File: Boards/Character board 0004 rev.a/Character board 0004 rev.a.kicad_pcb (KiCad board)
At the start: 2 copper layers, 184.3 x 186.8 mm, 64 parts, among them J1 card edge, J2 character connector, Q1 2N6125, U1 2.2K, U10 Unused DIP, U11 ULN2003A, U12 ULN2003A, U13 7406, U14 74LS42, U15 LM741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

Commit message: updated boards to have correct logos
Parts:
- added G1: GND, Evan's parts:PTT white, F.Cu at (72.4, 27.3)
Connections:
- net BCLK renamed aux1_AGC
- net UNUSED1 renamed aux2_AGC
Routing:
- net GND: track 578.6 -> 606.3 mm

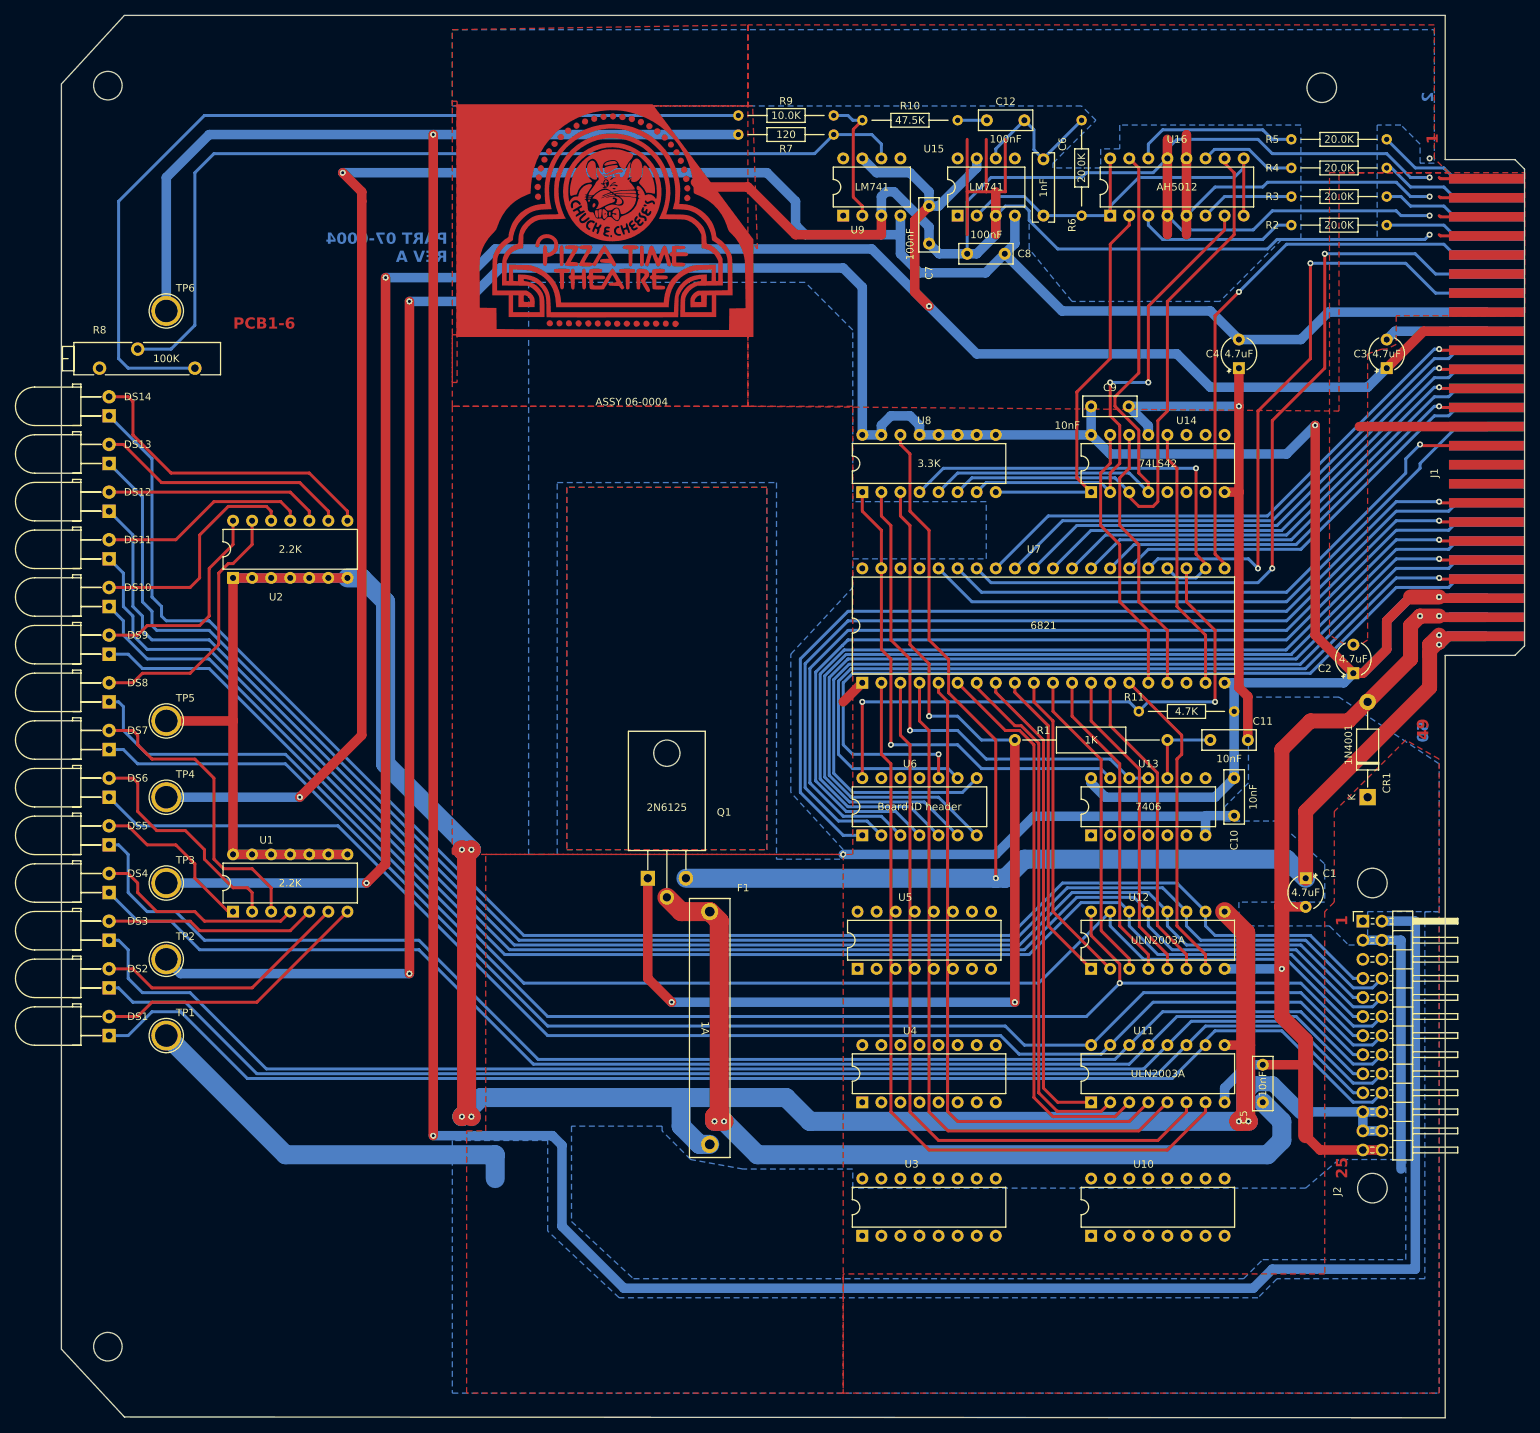
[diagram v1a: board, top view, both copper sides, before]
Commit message: revised LED spacing rev a
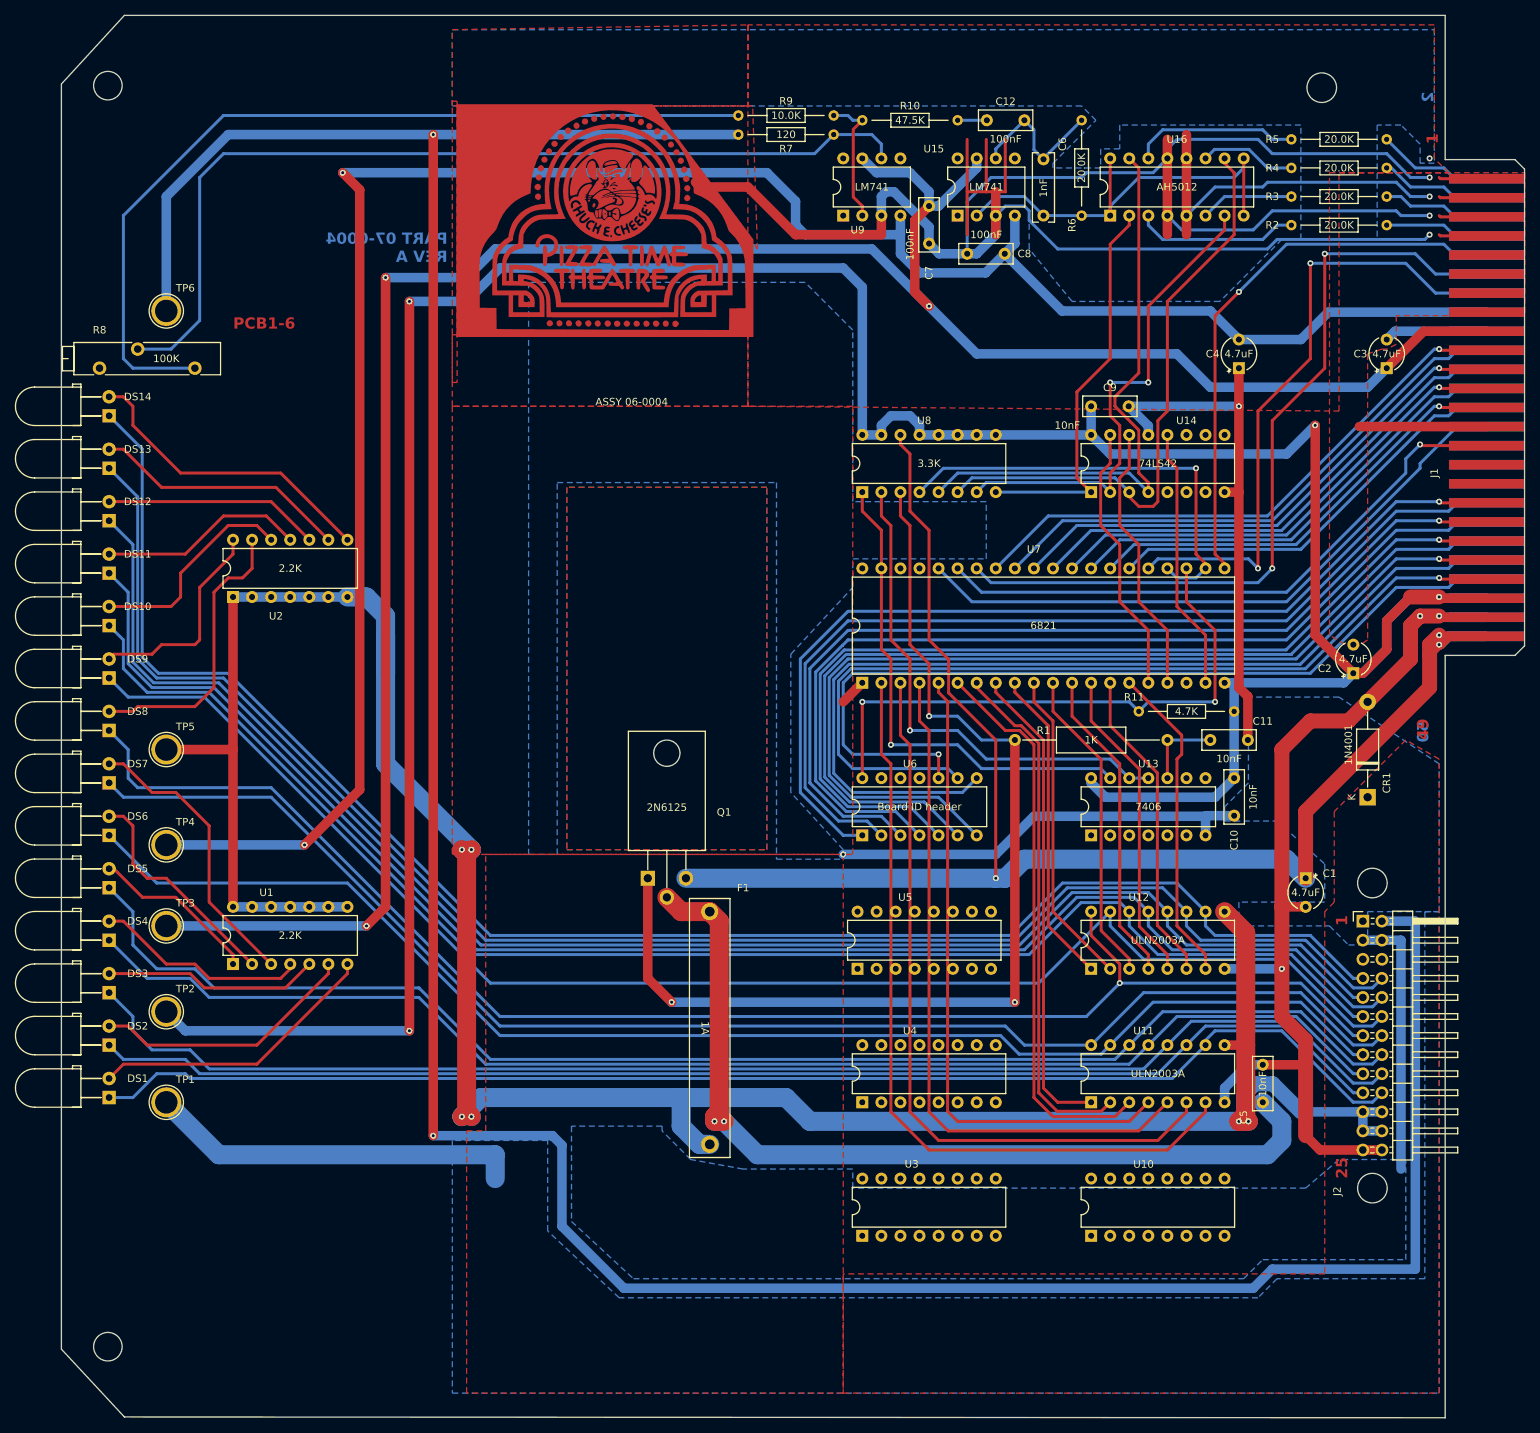
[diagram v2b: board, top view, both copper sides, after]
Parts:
- moved TP1 8.89 mm to (14.0, 144.8)
- moved DS1 8.25 mm to (6.35, 141.6)
- moved DS2 7.62 mm to (6.35, 134.6)
- moved DS3 6.98 mm to (6.35, 127.6)
- moved TP2 6.98 mm to (14.0, 132.7)
- moved U1 6.98 mm to (22.9, 126.4)
- moved DS4 6.35 mm to (6.35, 120.7)
- moved TP4 6.35 mm to (14.0, 110.5)
- moved DS5 5.72 mm to (6.35, 113.7)
- moved TP3 5.72 mm to (14.0, 121.3)
- moved DS6 5.08 mm to (6.35, 106.7)
- moved DS7 4.44 mm to (6.35, 99.7)
- moved TP5 3.81 mm to (14.0, 97.8)
- moved DS8 3.81 mm to (6.35, 92.7)
- moved DS9 3.17 mm to (6.35, 85.7)
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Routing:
- net 24Vout: track 362.9 -> 347.4 mm
- net 5V: track 409.1 -> 416.9 mm
- net -12V: track 282.1 -> 288.6 mm
- net 12V: track 304.6 -> 310.3 mm
- net B5out: track 216.5 -> 221.2 mm
- net A2out: track 185.4 -> 181.4 mm
- net GND: track 606.3 -> 602.6 mm
- net A0out: track 182.0 -> 178.6 mm
- net A1out: track 178.1 -> 174.9 mm
- net B4out: track 215.2 -> 218.3 mm
- net Net-(DS8-A): track 35.4 -> 38.2 mm
- net A4out: track 190.4 -> 187.7 mm
- net A3out: track 182.3 -> 179.6 mm
- net Net-(R8-Pad1): track 118.9 -> 116.5 mm
- net Net-(DS10-A): track 30.9 -> 28.7 mm
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
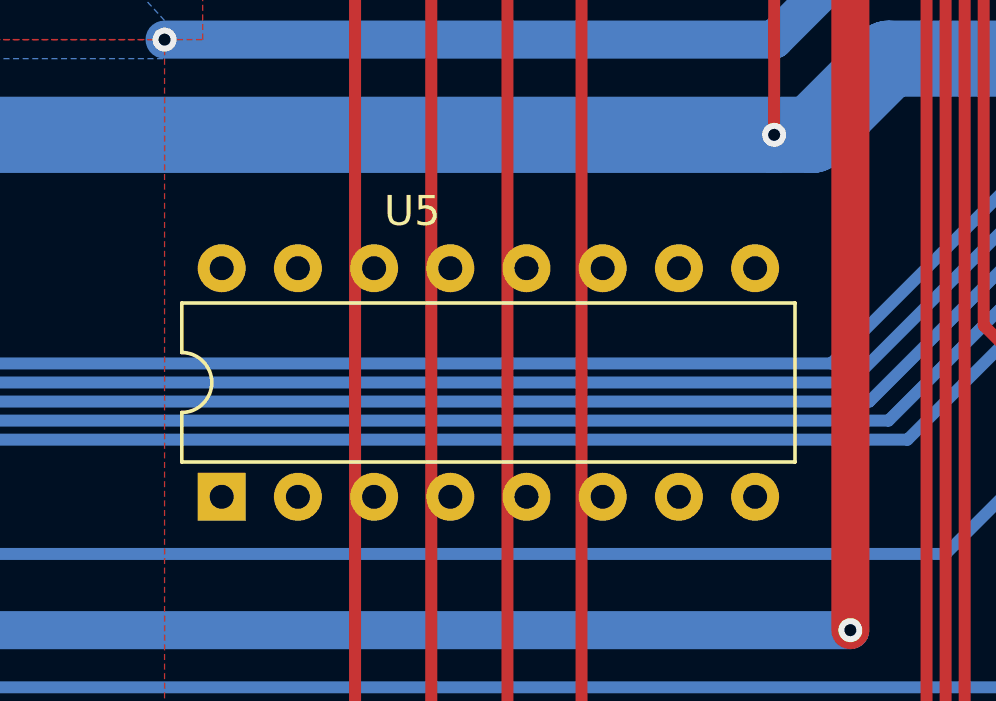
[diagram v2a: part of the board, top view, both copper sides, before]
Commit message: one chip misplaced
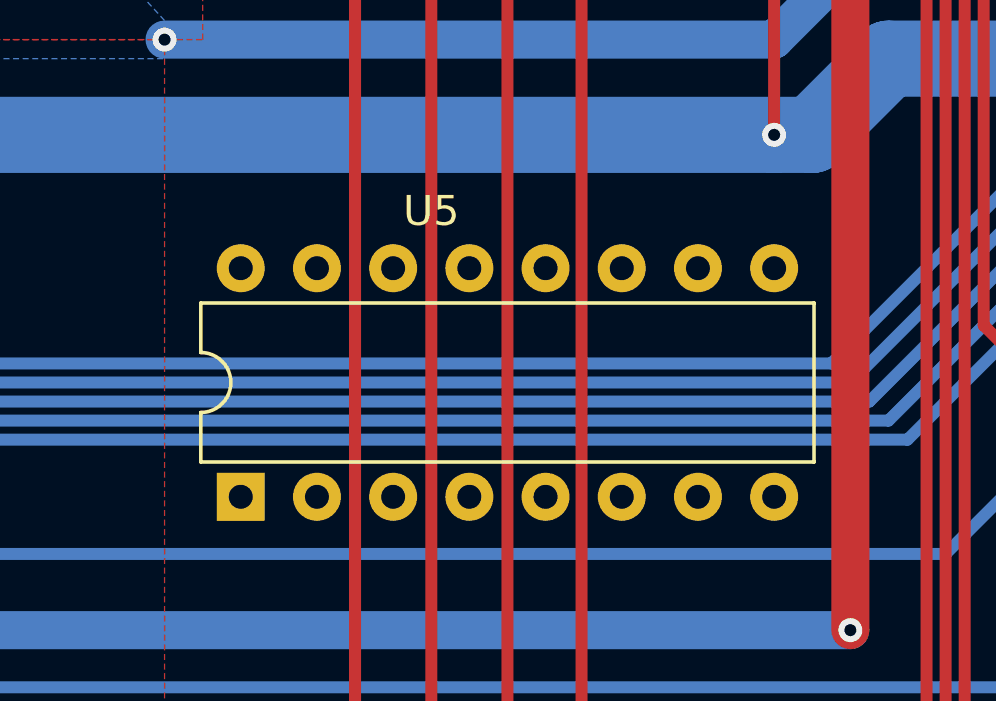
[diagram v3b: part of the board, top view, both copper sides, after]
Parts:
- moved U5 0.64 mm to (106.7, 127.0)
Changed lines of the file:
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@@
   )
   (footprint "Package_DIP:DIP-16_W7.62mm" (layer "F.Cu")
-    (at 106.045 127 90)
+    (at 106.68 127 90)
     (descr "16-lead though-hole mounted DIP package, row spacing 7.62 mm (300 mils)")
     (tags "THT DIP DIL PDIP 2.54mm 7.62mm 300mil")

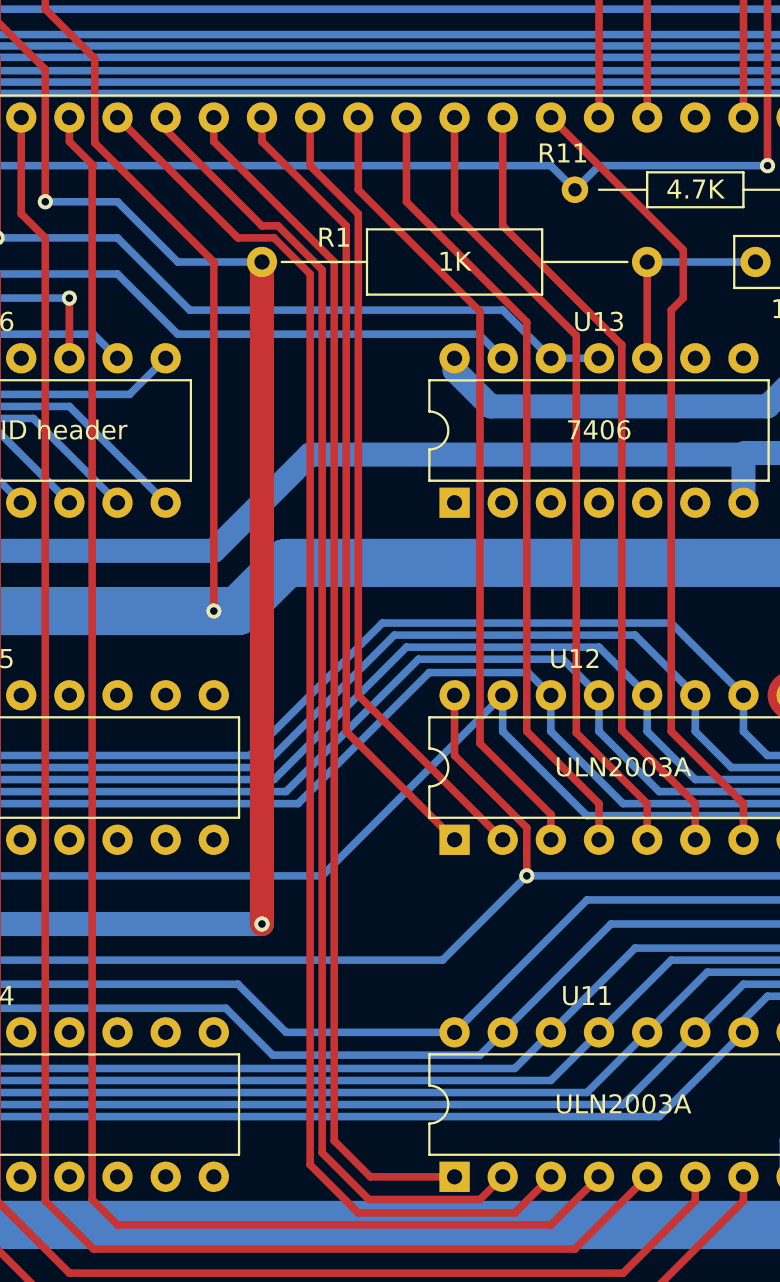
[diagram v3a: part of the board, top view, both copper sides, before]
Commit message: revisions from real life boards
tip130a is actually tip30a, widened holes for crystal, widened holes for big power resistor, fixed cpu board LED resistors
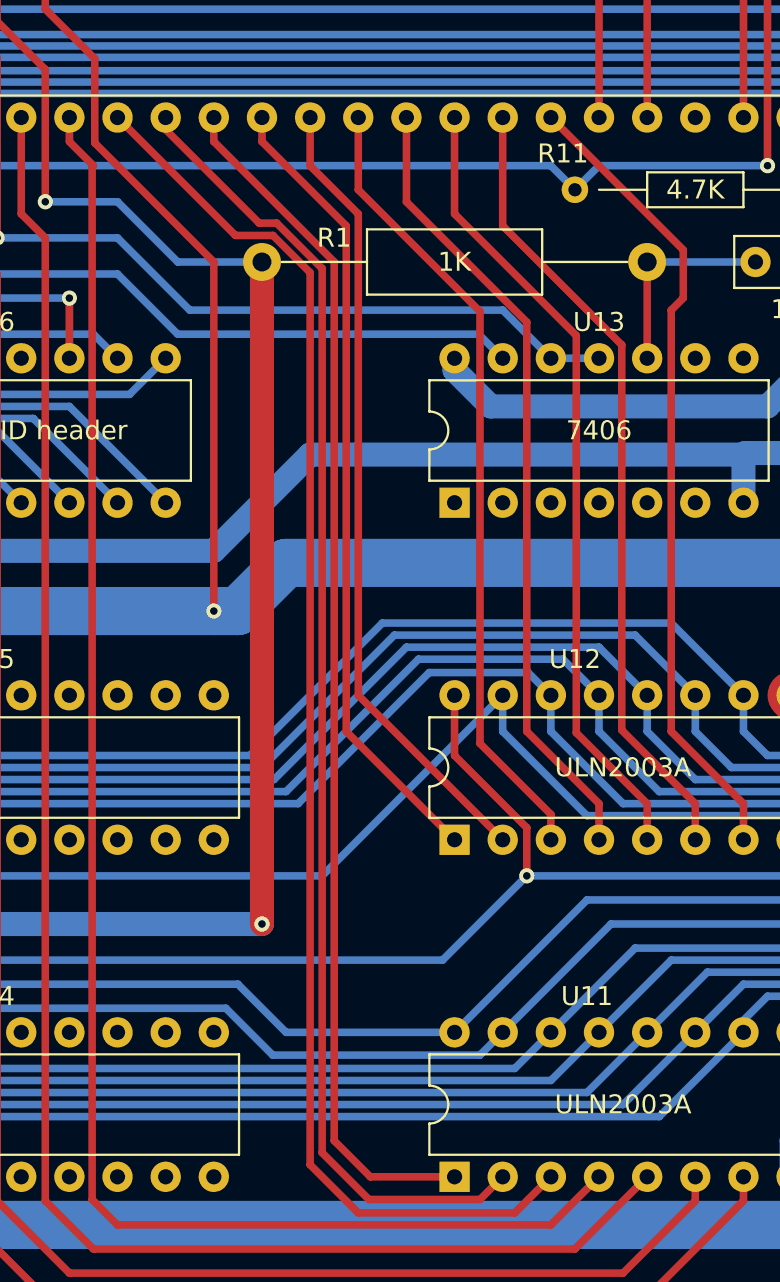
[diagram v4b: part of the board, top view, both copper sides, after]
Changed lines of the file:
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@@
     (fp_line (start 20.32 0) (end 14.66 0)
       (stroke (width 0.1) (type solid)) (layer "F.Fab"))
-    (pad "1" thru_hole circle (at 0 0) (size 1.6 1.6) (drill 0.8) (layers "*.Cu" "*.Mask")
+    (pad "1" thru_hole circle (at 0 0) (size 2 2) (drill 1) (layers "*.Cu" "*.Mask")
       (net 184 "24Vpu") (pintype "passive"))
-    (pad "2" thru_hole oval (at 20.32 0) (size 1.6 1.6) (drill 0.8) (layers "*.Cu" "*.Mask")
+    (pad "2" thru_hole circle (at 20.32 0) (size 2 2) (drill 1) (layers "*.Cu" "*.Mask")
       (net 182 "Net-(C11-Pad1)") (pintype "passive"))
     (model "${KICAD6_3DMODEL_DIR}/Resistor_THT.3dshapes/R_Axial_DIN0309_L9.0mm_D3.2mm_P20.32mm_Horizontal.wrl"
@@
   (segment (start 118.11 91.44) (end 118.04 91.51) (width 0.4) (layer "F.Cu") (net 170))
   (segment (start 116.84 90.17) (end 118.11 91.44) (width 0.4) (layer "F.Cu") (net 170))
-  (segment (start 119.38 88.9) (end 125.73 95.25) (width 0.4) (layer "F.Cu") (net 171))
-  (segment (start 125.73 95.25) (end 127.635 95.25) (width 0.4) (layer "F.Cu") (net 171))
-  (segment (start 132.08 146.685) (end 140.335 146.685) (width 0.4) (layer "F.Cu") (net 171))
-  (segment (start 140.335 146.685) (end 142.24 144.78) (width 0.4) (layer "F.Cu") (net 171))
   (segment (start 129.54 144.145) (end 132.08 146.685) (width 0.4) (layer "F.Cu") (net 171))
-  (segment (start 127.635 95.25) (end 129.54 97.155) (width 0.4) (layer "F.Cu") (net 171))
-  (segment (start 129.54 97.155) (end 129.54 144.145) (width 0.4) (layer "F.Cu") (net 171))
-  (segment (start 127.848528 94.615) (end 130.175 96.941472) (width 0.4) (layer "F.Cu") (net 172))
-  (segment (start 130.175 143.51) (end 132.645 145.98) (width 0.4) (layer "F.Cu") (net 172))
-  (segment (start 121.92 89.535) (end 127 94.615) (width 0.4) (layer "F.Cu") (net 172))
-  (segment (start 127 94.615) (end 127.848528 94.615) (width 0.4) (layer "F.Cu") (net 172))
-  (segment (start 130.175 96.941472) (end 130.175 143.51) (width 0.4) (layer "F.Cu") (net 172))
-  (segment (start 121.92 88.9) (end 121.92 89.535) (width 0.4) (layer "F.Cu") (net 172))
-  (segment (start 138.5 145.98) (end 139.7 144.78) (width 0.4) (layer "F.Cu") (net 172))
+  (segment (start 119.38 88.9) (end 125.6 95.12) (width 0.4) (layer "F.Cu") (net 171))
+  (segment (start 127.579899 95.12) (end 129.54 97.080101) (width 0.4) (layer "F.Cu") (net 171))
+  (segment (start 140.335 146.685) (end 142.24 144.78) (width 0.4) (layer "F.Cu") (net 171))
+  (segment (start 125.6 95.12) (end 127.579899 95.12) (width 0.4) (layer "F.Cu") (net 171))
+  (segment (start 132.08 146.685) (end 140.335 146.685) (width 0.4) (layer "F.Cu") (net 171))
+  (segment (start 129.54 97.080101) (end 129.54 144.145) (width 0.4) (layer "F.Cu") (net 171))
+  (segment (start 121.92 89.535) (end 126.855786 94.470786) (width 0.4) (layer "F.Cu") (net 172))
+  (segment (start 130.175 96.866573) (end 130.175 143.51) (width 0.4) (layer "F.Cu") (net 172))
   (segment (start 132.645 145.98) (end 138.5 145.98) (width 0.4) (layer "F.Cu") (net 172))
-  (segment (start 124.46 90.17) (end 130.81 96.52) (width 0.4) (layer "F.Cu") (net 173))
-  (segment (start 130.81 96.52) (end 130.81 142.875) (width 0.4) (layer "F.Cu") (net 173))
+  (segment (start 126.855786 94.470786) (end 127.779214 94.470786) (width 0.4) (layer "F.Cu") (net 172))
+  (segment (start 138.5 145.98) (end 139.7 144.78) (width 0.4) (layer "F.Cu") (net 172))
+  (segment (start 121.92 88.9) (end 121.92 89.535) (width 0.4) (layer "F.Cu") (net 172))
+  (segment (start 127.779214 94.470786) (end 130.175 96.866573) (width 0.4) (layer "F.Cu") (net 172))
+  (segment (start 130.175 143.51) (end 132.645 145.98) (width 0.4) (layer "F.Cu") (net 172))
   (segment (start 124.46 88.9) (end 124.46 90.17) (width 0.4) (layer "F.Cu") (net 173))
-  (segment (start 132.715 144.78) (end 137.16 144.78) (width 0.4) (layer "F.Cu") (net 173))
   (segment (start 130.81 142.875) (end 132.715 144.78) (width 0.4) (layer "F.Cu") (net 173))
+  (segment (start 124.46 90.17) (end 130.81 96.52) (width 0.4) (layer "F.Cu") (net 173))
+  (segment (start 132.715 144.78) (end 137.16 144.78) (width 0.4) (layer "F.Cu") (net 173))
+  (segment (start 130.81 96.52) (end 130.81 142.875) (width 0.4) (layer "F.Cu") (net 173))
   (segment (start 131.445 94.615) (end 131.445 121.285) (width 0.4) (layer "F.Cu") (net 174))
   (segment (start 127 88.9) (end 127 90.17) (width 0.4) (layer "F.Cu") (net 174))
